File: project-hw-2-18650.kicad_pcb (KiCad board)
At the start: 2 copper layers, 98 x 44 mm, 13 parts, among them J1 2060-452_998-404, U1 TPS62933

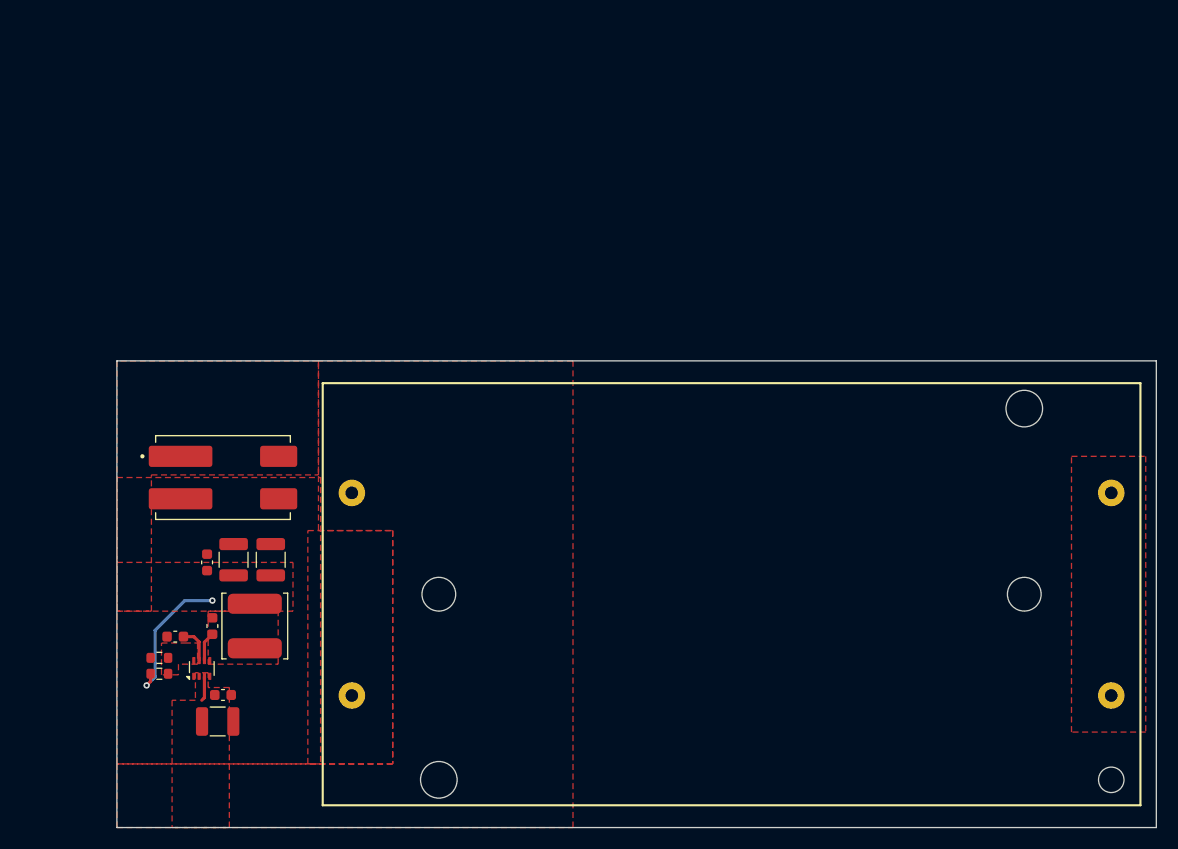
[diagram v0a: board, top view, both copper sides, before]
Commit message: pcb: change DNI footprint
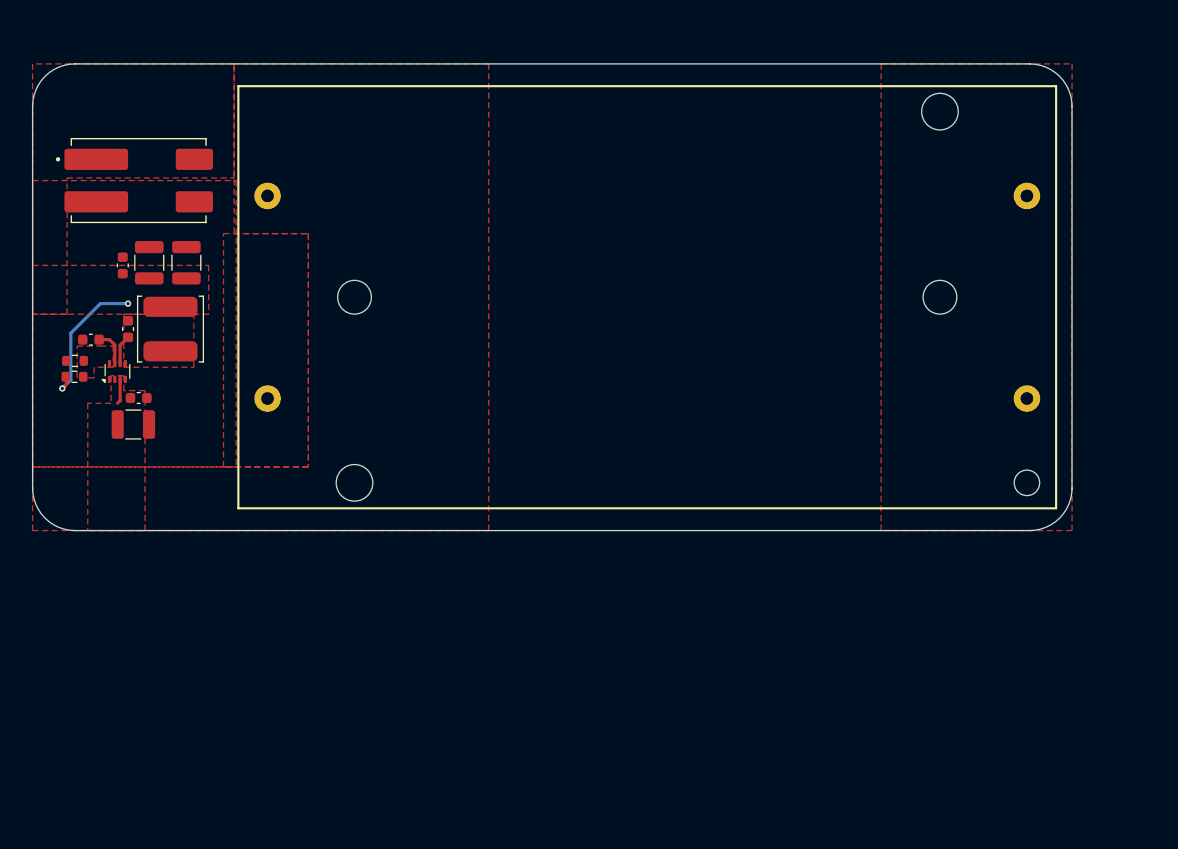
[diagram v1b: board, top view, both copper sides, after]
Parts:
- R1: footprint Resistor_SMD:R_0603_1608Metric -> SMD:0603_1608Metric_DNI_NoPaste
- moved R1 29.1 mm to (23.0, 49.5)
- moved BT1 29.1 mm to (77.0, 42.0)
- moved C1 29.1 mm to (28.6, 54.0)
- moved C2 29.1 mm to (29.1, 51.5)
- moved C3 29.1 mm to (24.6, 46.0)
- moved C4 29.1 mm to (28.1, 45.0)
- moved C5 29.1 mm to (27.6, 39.0)
- moved C6 29.1 mm to (33.5, 38.8)
- moved C7 29.1 mm to (30.1, 38.8)
- moved J1 29.1 mm to (29.1, 31.0)
- moved L1 29.1 mm to (32.0, 45.0)
- moved R2 29.1 mm to (23.1, 48.0)
- moved U1 29.1 mm to (27.1, 49.0)
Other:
- outline, holes or cut-outs redrawn

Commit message: pcb: add ground backplane
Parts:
- added H1: MountingHole_Pad, MountingHole:MountingHole_3.2mm_M3_ISO14580_Pad, F.Cu at (22.0, 20.0)
- added H2: MountingHole_Pad, MountingHole:MountingHole_3.2mm_M3_ISO14580_Pad, F.Cu at (22.0, 56.0)
- moved J1 4.15 mm to (27.9, 27.0)
- moved C1 4.14 mm to (27.5, 50.0)
- moved C2 4.14 mm to (28.0, 47.5)
- moved C3 4.14 mm to (23.5, 42.0)
- moved C4 4.14 mm to (27.0, 41.0)
- moved C5 4.14 mm to (26.5, 35.0)
- moved C7 4.14 mm to (29.0, 34.8)
- moved R2 4.14 mm to (22.0, 44.0)
- moved U1 4.14 mm to (26.0, 45.0)
- moved C6 4.14 mm to (32.5, 34.8)
- moved L1 4.14 mm to (31.0, 41.0)
- moved BT1 4.12 mm to (76.0, 38.0)
- moved R1 4.12 mm to (22.0, 45.5)
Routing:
- net /TPS6293x Converter/Vout: track 13.3 -> 14.5 mm
- net GND: vias 0 -> 24
- added copper zone on B.Cu, net GND

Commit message: pcb: routing v2
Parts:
- H1: value MountingHole_Pad -> MountingHole; footprint MountingHole:MountingHole_3.2mm_M3_ISO14580_Pad -> MountingHole:MountingHole_3.2mm_M3_ISO14580
- moved J1 20.0 mm to (27.0, 47.0)
- moved R1 19.9 mm to (28.0, 26.5), turned to -90 degrees
- moved C1 19.5 mm to (22.0, 31.2), turned to -90 degrees
- moved C2 17.4 mm to (24.5, 30.5), turned to -90 degrees
- moved R2 17.1 mm to (25.5, 27.2)
- moved C3 16.8 mm to (30.0, 26.5), turned to 90 degrees
- moved U1 15.0 mm to (27.0, 30.0), turned to 0 degrees
- moved C4 11.9 mm to (30.0, 29.5), turned to -90 degrees
- moved C6 8.28 mm to (25.2, 38.8), turned to 180 degrees
- moved L1 6.58 mm to (32.0, 34.5), turned to -90 degrees
- moved C7 3.82 mm to (25.2, 35.5), turned to 180 degrees
- moved C5 2.06 mm to (26.0, 33.0), turned to 180 degrees
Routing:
- net /TPS6293x Converter/Vout: track 14.5 -> 34.2 mm
- net Net-(U1-FB): track 0.00 -> 3.74 mm
- net +BATT: track 2.36 -> 0.00 mm
- net GND: vias 24 -> 21
- removed copper zone on F.Cu, net Net-(U1-FB)
